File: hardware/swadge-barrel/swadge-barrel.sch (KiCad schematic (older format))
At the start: 48 parts, among them J1 USB_B_Micro, Q1 Q_NPN_BEC, SW1 SW_SPDT, U1 ESP-13-WROOM-02D, U2 OLED_DISPLAY, U3 BUS_PCIexpress, U4 QMA6981, U5 AP1117-33, U6 OLED_CONNECTOR

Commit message: Barrel BOM
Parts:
- C4, C5, C6, C9: Notes 1206 Package, must be at least 1.5mm tall, may be taller. 1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 -> 1206 Package. must be at least 1.5mm tall. may be taller. 1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
- D1, D2, D3, D4, D5, D6: Notes Use WS2812B LED, Digikey item is x10 -> Use WS2812B LED. Digikey item is x10
- LS1: Digikey https://lcsc.com/product-detail/Buzzers_Jiangsu-Huaneng-Ele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 -> LCSC Part #C96102; Notes Use magnetic buzzer, 3V rated, 9mm diameter, 5mm between th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 -> Use magnetic buzzer. 3V rated. 9mm diameter. 5mm between th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
- Q1: Notes Use any NPN transistor in SOT-23 package with the same leads as BC848BLT3G (1=base, 2=emitter, 3=collector) -> Use any NPN transistor in SOT-23 package with the same leads as BC848BLT3G (1=base. 2=emitter. 3=collector)
- R8, R9: Notes 0603 Package, must not be taller than 0.8mm, this sits unde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 -> 0603 Package. must not be taller than 0.8mm. this sits unde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
- S2, S3: Digikey https://www.digikey.com/product-detail/en/omron-electronics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 -> SW1278CT-ND
- U2: Notes Must be a single color, white. Must have SSD1306 driver. Mu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 -> Must be a single color. white. Must have SSD1306 driver. Mu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
- U6: Notes Must have top contacts, same as the OLED -> Must have top contacts. same as the OLED
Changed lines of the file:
@@
 EESchema Schematic File Version 4
-LIBS:swadge-barrel-cache
 EELAYER 29 0
 EELAYER END
@@
 F 4 "45" H 0   0   50  0001 C CNN "Cost100"
 F 5 "1528-1104-ND" H 0   0   50  0001 C CNN "Digikey"
-F 6 "Use WS2812B LED, Digikey item is x10" H 0   0   50  0001 C CNN "Notes"
+F 6 "Use WS2812B LED. Digikey item is x10" H 0   0   50  0001 C CNN "Notes"
 F 7 "Y" H 0   0   50  0001 C CNN "Substitutable"
 	1    4300 1650
@@
 F 4 "45" H 0   0   50  0001 C CNN "Cost100"
 F 5 "1528-1104-ND" H 0   0   50  0001 C CNN "Digikey"
-F 6 "Use WS2812B LED, Digikey item is x10" H 0   0   50  0001 C CNN "Notes"
+F 6 "Use WS2812B LED. Digikey item is x10" H 0   0   50  0001 C CNN "Notes"
 F 7 "Y" H 0   0   50  0001 C CNN "Substitutable"
 	1    4950 1650
@@
 F 4 "45" H 0   0   50  0001 C CNN "Cost100"
 F 5 "1528-1104-ND" H 0   0   50  0001 C CNN "Digikey"
-F 6 "Use WS2812B LED, Digikey item is x10" H 0   0   50  0001 C CNN "Notes"
+F 6 "Use WS2812B LED. Digikey item is x10" H 0   0   50  0001 C CNN "Notes"
 F 7 "Y" H 0   0   50  0001 C CNN "Substitutable"
 	1    5600 1650
@@
 F 4 "45" H 0   0   50  0001 C CNN "Cost100"
 F 5 "1528-1104-ND" H 0   0   50  0001 C CNN "Digikey"
-F 6 "Use WS2812B LED, Digikey item is x10" H 0   0   50  0001 C CNN "Notes"
+F 6 "Use WS2812B LED. Digikey item is x10" H 0   0   50  0001 C CNN "Notes"
 F 7 "Y" H 0   0   50  0001 C CNN "Substitutable"
 	1    6250 1650
@@
 F 4 "45" H 0   0   50  0001 C CNN "Cost100"
 F 5 "1528-1104-ND" H 0   0   50  0001 C CNN "Digikey"
-F 6 "Use WS2812B LED, Digikey item is x10" H 0   0   50  0001 C CNN "Notes"
+F 6 "Use WS2812B LED. Digikey item is x10" H 0   0   50  0001 C CNN "Notes"
 F 7 "Y" H 0   0   50  0001 C CNN "Substitutable"
 	1    6900 1650
@@
 F 4 "45" H 0   0   50  0001 C CNN "Cost100"
 F 5 "1528-1104-ND" H 0   0   50  0001 C CNN "Digikey"
-F 6 "Use WS2812B LED, Digikey item is x10" H 0   0   50  0001 C CNN "Notes"
+F 6 "Use WS2812B LED. Digikey item is x10" H 0   0   50  0001 C CNN "Notes"
 F 7 "Y" H 0   0   50  0001 C CNN "Substitutable"
 	1    7550 1650
@@
 F 5 "1276-1097-1-ND" H 0   0   50  0001 C CNN "Digikey"
 F 6 "Y" H 0   0   50  0001 C CNN "Substitutable"
-F 7 "1206 Package, must be at least 1.5mm tall, may be taller. 1.8mm is common and preferrable. This protects the OLED's corners" H 4150 3600 50  0001 C CNN "Notes"
+F 7 "1206 Package. must be at least 1.5mm tall. may be taller. 1.8mm is common and preferable. This protects the OLED's corners" H 4150 3600 50  0001 C CNN "Notes"
 	1    4150 3600
 	-1   0    0    1
@@
 F 5 "1276-1097-1-ND" H 0   0   50  0001 C CNN "Digikey"
 F 6 "Y" H 0   0   50  0001 C CNN "Substitutable"
-F 7 "1206 Package, must be at least 1.5mm tall, may be taller. 1.8mm is common and preferrable. This protects the OLED's corners" H 4000 3300 50  0001 C CNN "Notes"
+F 7 "1206 Package. must be at least 1.5mm tall. may be taller. 1.8mm is common and preferable. This protects the OLED's corners" H 4000 3300 50  0001 C CNN "Notes"
 	1    4000 3300
 	-1   0    0    1
@@
 F 5 "1276-1097-1-ND" H 0   0   50  0001 C CNN "Digikey"
 F 6 "Y" H 0   0   50  0001 C CNN "Substitutable"
-F 7 "1206 Package, must be at least 1.5mm tall, may be taller. 1.8mm is common and preferrable. This protects the OLED's corners" H 4450 2700 50  0001 C CNN "Notes"
+F 7 "1206 Package. must be at least 1.5mm tall. may be taller. 1.8mm is common and preferable. This protects the OLED's corners" H 4450 2700 50  0001 C CNN "Notes"
 	1    4450 2700
 	1    0    0    -1
@@
 F 5 "1276-1097-1-ND" H 0   0   50  0001 C CNN "Digikey"
 F 6 "Y" H 0   0   50  0001 C CNN "Substitutable"
-F 7 "1206 Package, must be at least 1.5mm tall, may be taller. 1.8mm is common and preferrable. This protects the OLED's corners" H 4050 2900 50  0001 C CNN "Notes"
+F 7 "1206 Package. must be at least 1.5mm tall. may be taller. 1.8mm is common and preferable. This protects the OLED's corners" H 4050 2900 50  0001 C CNN "Notes"
 	1    4050 2900
 	1    0    0    -1
@@
 F 1 "B3FS-4002P" H 2775 1284 50  0000 C CNN
 F 2 "Swadge_Parts:B3FS4002P" H 2750 1600 50  0001 L CNN
-F 3 "http://omronfs.omron.com/en_US/ecb/products/pdf/en-b3fs_4.pdf" H 3100 1150 50  0001 L CNN
-F 4 "https://www.digikey.com/product-detail/en/omron-electronics-inc-emc-div/B3FS-4002P/SW1278TR-ND/2772023" H 2800 1750 50  0001 C CNN "Digikey"
+F 3 "https://omronfs.omron.com/en_US/ecb/products/pdf/en-b3fs_4.pdf" H 3100 1150 50  0001 L CNN
+F 4 "SW1278CT-ND" H 2800 1750 50  0001 C CNN "Digikey"
 F 5 "76" H 2600 1600 50  0001 C CNN "Cost100"
 F 6 "Y" H 2450 1650 50  0001 C CNN "Substitutable"
@@
 F 1 "B3FS-4002P" H 1425 1284 50  0000 C CNN
 F 2 "Swadge_Parts:B3FS4002P" H 1400 1600 50  0001 L CNN
-F 3 "http://omronfs.omron.com/en_US/ecb/products/pdf/en-b3fs_4.pdf" H 1750 1150 50  0001 L CNN
-F 4 "https://www.digikey.com/product-detail/en/omron-electronics-inc-emc-div/B3FS-4002P/SW1278TR-ND/2772023" H 1450 1750 50  0001 C CNN "Digikey"
+F 3 "https://omronfs.omron.com/en_US/ecb/products/pdf/en-b3fs_4.pdf" H 1750 1150 50  0001 L CNN
+F 4 "SW1278CT-ND" H 1450 1750 50  0001 C CNN "Digikey"
 F 5 "76" H 1250 1600 50  0001 C CNN "Cost100"
 F 6 "Y" H 1100 1650 50  0001 C CNN "Substitutable"
@@
 F 5 "1.554" H 1750 7400 50  0001 C CNN "Cost100"
 F 6 "Y" H 1700 7500 50  0001 C CNN "Substitutable"
-F 7 "Use any NPN transistor in SOT-23 package with the same leads as BC848BLT3G (1=base, 2=emitter, 3=collector)" H 1400 6950 50  0001 C CNN "Notes"
+F 7 "Use any NPN transistor in SOT-23 package with the same leads as BC848BLT3G (1=base. 2=emitter. 3=collector)" H 1400 6950 50  0001 C CNN "Notes"
 	1    1400 6950
 	1    0    0    -1
@@
 F 2 "Swadge_Parts:Buzzer_12x9.5RM7.6" H 1700 6350 50  0001 C CNN
 F 3 "https://datasheet.lcsc.com/szlcsc/Jiangsu-Huaneng-Elec-HNB09A03_C96102.pdf" H 1690 6500 50  0001 C CNN
-F 4 "https://lcsc.com/product-detail/Buzzers_Jiangsu-Huaneng-Elec-HNB09A03_C96102.html" H 1300 6900 50  0001 C CNN "Digikey"
+F 4 "LCSC Part #C96102" H 1300 6900 50  0001 C CNN "Digikey"
 F 5 "13.48" H 1950 6800 50  0001 C CNN "Cost100"
 F 6 "Y" H 1950 7050 50  0001 C CNN "Substitutable"
-F 7 "Use magnetic buzzer, 3V rated, 9mm diameter, 5mm between the leads" H 1400 7000 50  0001 C CNN "Notes"
+F 7 "Use magnetic buzzer. 3V rated. 9mm diameter. 5mm between the leads" H 1400 7000 50  0001 C CNN "Notes"
 	1    1700 6550
 	1    0    0    -1
@@
 F 5 "10" H 2600 6400 10  0001 C CNN "Cost100"
 F 6 "Y" H 2600 6400 10  0001 C CNN "Substitutable"
-F 7 "0603 Package, must not be taller than 0.8mm, this sits under part of the OLED" H 2600 6400 50  0001 C CNN "Notes"
+F 7 "0603 Package. must not be taller than 0.8mm. this sits under part of the OLED" H 2600 6400 50  0001 C CNN "Notes"
 	1    2600 6400
 	1    0    0    -1
@@
 F 5 "10" H 2950 6400 10  0001 C CNN "Cost100"
 F 6 "Y" H 2950 6400 10  0001 C CNN "Substitutable"
-F 7 "0603 Package, must not be taller than 0.8mm, this sits under part of the OLED" H 2950 6400 50  0001 C CNN "Notes"
+F 7 "0603 Package. must not be taller than 0.8mm. this sits under part of the OLED" H 2950 6400 50  0001 C CNN "Notes"
 	1    2950 6400
 	1    0    0    -1
@@
 F 5 "LCSC #C11095" H 0   0   50  0001 C CNN "Digikey"
 F 6 "Y" H 0   0   50  0001 C CNN "Substitutable"
-F 7 "Must have top contacts, same as the OLED" H 5950 4050 50  0001 C CNN "Notes"
+F 7 "Must have top contacts. same as the OLED" H 5950 4050 50  0001 C CNN "Notes"
 	1    5950 4050
 	1    0    0    -1
@@
 F 6 "352" H 5100 6500 50  0001 C CNN "Cost100"
 F 7 "Y" H 5100 6500 50  0001 C CNN "Substitutable"
-F 8 "Must be a single color, white. Must have SSD1306 driver. Must have top pins, 0.5mm pitch, like the connector" H 5100 6500 50  0001 C CNN "Notes"
+F 8 "Must be a single color. white. Must have SSD1306 driver. Must have top pins. 0.5mm pitch. like the connector" H 5100 6500 50  0001 C CNN "Notes"
 	1    5100 6500
 	1    0    0    -1

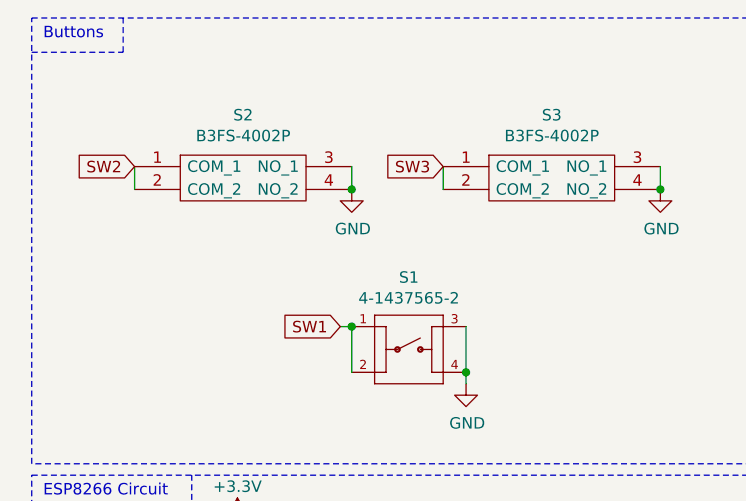
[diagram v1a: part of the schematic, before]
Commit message: #26 Remapped buttons to match devkit gpios
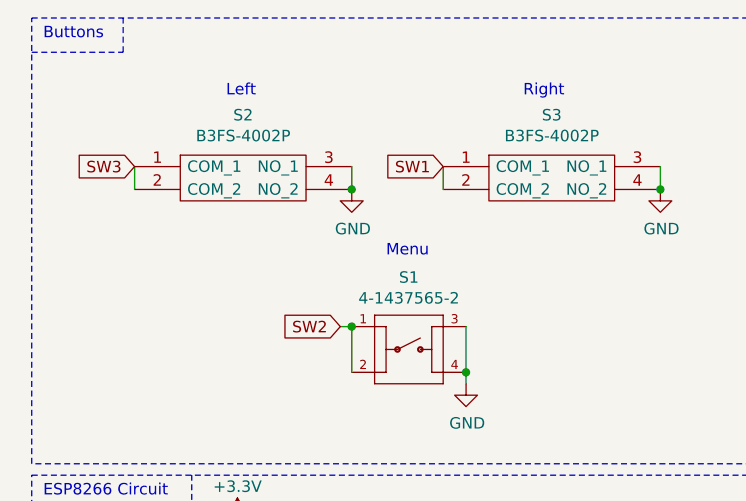
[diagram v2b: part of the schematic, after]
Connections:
- net SW1: now also S3.1 (COM_1), S3.2 (COM_2); no longer S1.1, S1.2
- net SW2: now also S1.1, S1.2; no longer S2.1 (COM_1), S2.2 (COM_2)
- net SW3: now also S2.1 (COM_1), S2.2 (COM_2); no longer S3.1 (COM_1), S3.2 (COM_2)
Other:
- note added: "Left"
- note added: "Menu"
- note added: "Right"
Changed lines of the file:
@@
 EESchema Schematic File Version 4
+LIBS:swadge-barrel-cache
 EELAYER 29 0
 EELAYER END
@@
 Wire Notes Line
 	10000 650  10000 500
-Text GLabel 1850 1850 0    50   Input ~ 0
+Text GLabel 2300 1150 0    50   Input ~ 0
 SW1
 $Comp
@@
 	1    0    0    -1
 $EndComp
-Text GLabel 2300 1150 0    50   Input ~ 0
+Text GLabel 950  1150 0    50   Input ~ 0
 SW3
-Text GLabel 950  1150 0    50   Input ~ 0
+Text GLabel 1850 1850 0    50   Input ~ 0
 SW2
 Connection ~ 1900 1850
@@
 	1    0    0    -1
 $EndComp
+Text Notes 1350 850  0    50   ~ 0
+Left
+Text Notes 2650 850  0    50   ~ 0
+Right
+Text Notes 2050 1550 0    50   ~ 0
+Menu
 $EndSCHEMATC

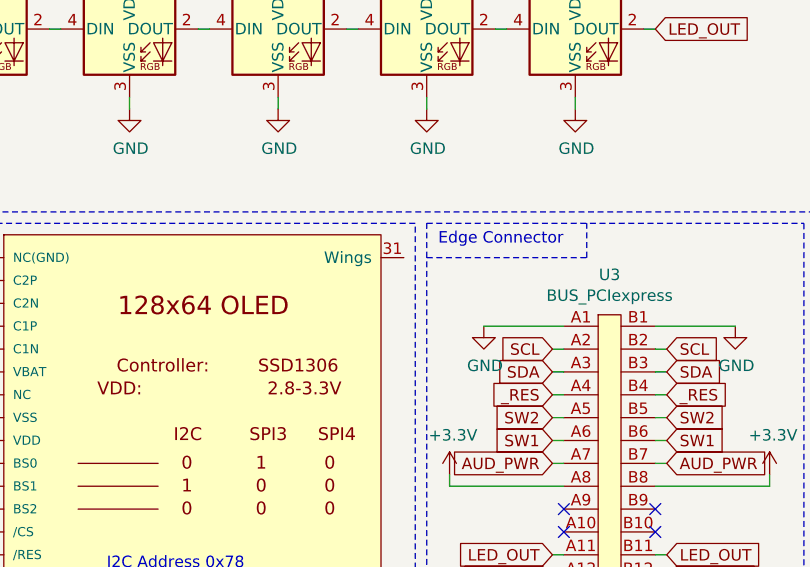
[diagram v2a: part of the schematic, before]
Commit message: Flipped OLED contacts, haven't routed them yet #24
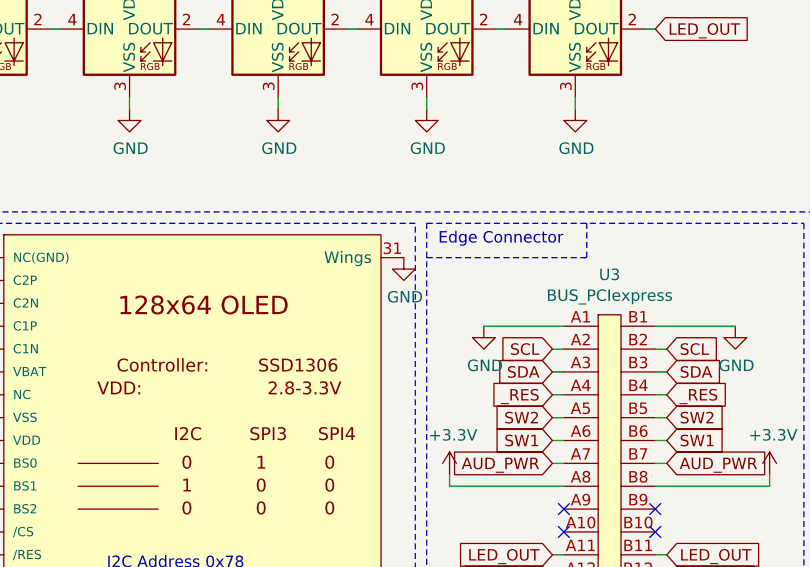
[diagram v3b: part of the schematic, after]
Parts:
- U6: footprint Swadge_Parts:oled-flat_copy -> Swadge_Parts:ER-OLED0.96-1.3
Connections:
- net GND: now also U6.31 (Wings)
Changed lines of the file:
@@
 F 0 "U6" H 5100 2300 45  0000 L CNN
 F 1 "OLED_CONNECTOR" H 5100 2400 45  0000 L CNN
-F 2 "Swadge_Parts:oled-flat_copy" H 5980 4200 20  0001 C CNN
+F 2 "Swadge_Parts:ER-OLED0.96-1.3" H 5980 4200 20  0001 C CNN
 F 3 "https://datasheet.lcsc.com/szlcsc/JUSHUO-AFC07-S30ECC-00_C11095.pdf" H 5950 4050 50  0001 C CNN
 F 4 "119" H 0   0   50  0001 C CNN "Cost100"
@@
 Text Notes 2050 1550 0    50   ~ 0
 Menu
+$Comp
+L power:GND #PWR?
+U 1 1 5D809654
+P 6800 2650
+F 0 "#PWR?" H 6800 2400 50  0001 C CNN
+F 1 "GND" H 6805 2477 50  0000 C CNN
+F 2 "" H 6800 2650 50  0001 C CNN
+F 3 "" H 6800 2650 50  0001 C CNN
+	1    6800 2650
+	1    0    0    -1
+$EndComp
 $EndSCHEMATC

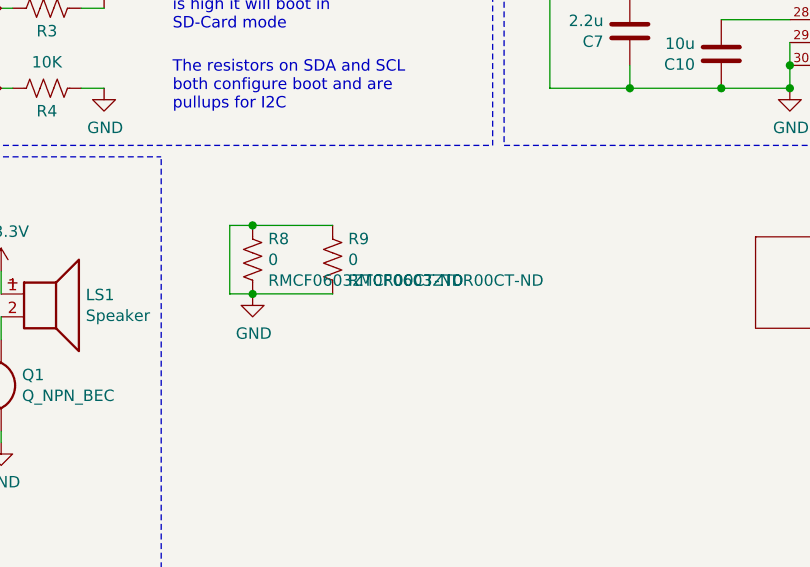
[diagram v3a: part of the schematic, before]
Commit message: #24 Rerouted OLED traces
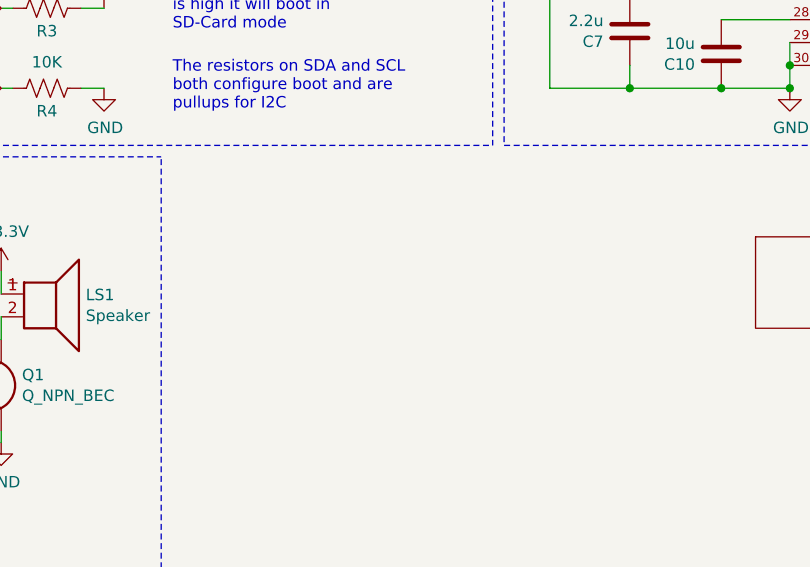
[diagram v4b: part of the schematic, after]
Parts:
- removed R8, R9: 0, Swadge_Parts:R_0603_1608Metric, symbol Swadge_Parts:R_US
- C4, C5, C6, C9: footprint Swadge_Parts:C_1206_3216Metric -> Swadge_Parts:C_0603_1608Metric; Digikey 1276-1097-1-ND -> 1276-1036-1-ND; Notes 1206 Package. must be at least 1.5mm tall. may be taller. 1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 -> 0603 Package
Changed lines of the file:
@@
 F 0 "C6" H 3850 3650 50  0000 L CNN
 F 1 "1u" H 3850 3550 50  0000 L CNN
-F 2 "Swadge_Parts:C_1206_3216Metric" H 4188 3450 50  0001 C CNN
+F 2 "Swadge_Parts:C_0603_1608Metric" H 4188 3450 50  0001 C CNN
 F 3 "" H 4150 3600 50  0001 C CNN
 F 4 "10" H 0   0   50  0001 C CNN "Cost100"
-F 5 "1276-1097-1-ND" H 0   0   50  0001 C CNN "Digikey"
+F 5 "1276-1036-1-ND" H 0   0   50  0001 C CNN "Digikey"
 F 6 "Y" H 0   0   50  0001 C CNN "Substitutable"
-F 7 "1206 Package. must be at least 1.5mm tall. may be taller. 1.8mm is common and preferable. This protects the OLED's corners" H 4150 3600 50  0001 C CNN "Notes"
+F 7 "0603 Package" H 4150 3600 50  0001 C CNN "Notes"
 	1    4150 3600
 	-1   0    0    1
@@
 F 0 "C4" H 4115 3346 50  0000 L CNN
 F 1 "1u" H 4115 3255 50  0000 L CNN
-F 2 "Swadge_Parts:C_1206_3216Metric" H 4038 3150 50  0001 C CNN
+F 2 "Swadge_Parts:C_0603_1608Metric" H 4038 3150 50  0001 C CNN
 F 3 "" H 4000 3300 50  0001 C CNN
 F 4 "10" H 0   0   50  0001 C CNN "Cost100"
-F 5 "1276-1097-1-ND" H 0   0   50  0001 C CNN "Digikey"
+F 5 "1276-1036-1-ND" H 0   0   50  0001 C CNN "Digikey"
 F 6 "Y" H 0   0   50  0001 C CNN "Substitutable"
-F 7 "1206 Package. must be at least 1.5mm tall. may be taller. 1.8mm is common and preferable. This protects the OLED's corners" H 4000 3300 50  0001 C CNN "Notes"
+F 7 "0603 Package" H 4000 3300 50  0001 C CNN "Notes"
 	1    4000 3300
 	-1   0    0    1
@@
 F 0 "C9" H 4565 2746 50  0000 L CNN
 F 1 "1u" H 4565 2655 50  0000 L CNN
-F 2 "Swadge_Parts:C_1206_3216Metric" H 4488 2550 50  0001 C CNN
+F 2 "Swadge_Parts:C_0603_1608Metric" H 4488 2550 50  0001 C CNN
 F 3 "" H 4450 2700 50  0001 C CNN
 F 4 "10" H 0   0   50  0001 C CNN "Cost100"
-F 5 "1276-1097-1-ND" H 0   0   50  0001 C CNN "Digikey"
+F 5 "1276-1036-1-ND" H 0   0   50  0001 C CNN "Digikey"
 F 6 "Y" H 0   0   50  0001 C CNN "Substitutable"
-F 7 "1206 Package. must be at least 1.5mm tall. may be taller. 1.8mm is common and preferable. This protects the OLED's corners" H 4450 2700 50  0001 C CNN "Notes"
+F 7 "0603 Package" H 4450 2700 50  0001 C CNN "Notes"
 	1    4450 2700
 	1    0    0    -1
@@
 F 0 "C5" H 4165 2946 50  0000 L CNN
 F 1 "1u" H 4165 2855 50  0000 L CNN
-F 2 "Swadge_Parts:C_1206_3216Metric" H 4088 2750 50  0001 C CNN
+F 2 "Swadge_Parts:C_0603_1608Metric" H 4088 2750 50  0001 C CNN
 F 3 "" H 4050 2900 50  0001 C CNN
 F 4 "10" H 0   0   50  0001 C CNN "Cost100"
-F 5 "1276-1097-1-ND" H 0   0   50  0001 C CNN "Digikey"
+F 5 "1276-1036-1-ND" H 0   0   50  0001 C CNN "Digikey"
 F 6 "Y" H 0   0   50  0001 C CNN "Substitutable"
-F 7 "1206 Package. must be at least 1.5mm tall. may be taller. 1.8mm is common and preferable. This protects the OLED's corners" H 4050 2900 50  0001 C CNN "Notes"
+F 7 "0603 Package" H 4050 2900 50  0001 C CNN "Notes"
 	1    4050 2900
 	1    0    0    -1
@@
 Wire Notes Line
 	500  7750 2200 7750
-$Comp
-L Swadge_Parts:R_US R8
-U 1 1 5D6E1A5B
-P 2600 6400
-F 0 "R8" H 2668 6491 50  0000 L CNN
-F 1 "0" H 2668 6400 50  0000 L CNN
-F 2 "Swadge_Parts:R_0603_1608Metric" V 2640 6390 50  0001 C CNN
-F 3 "~" V 2700 6400 50  0001 C CNN
-F 4 "RMCF0603ZT0R00CT-ND" H 2668 6309 50  0000 L CNN "Digikey"
-F 5 "10" H 2600 6400 10  0001 C CNN "Cost100"
-F 6 "Y" H 2600 6400 10  0001 C CNN "Substitutable"
-F 7 "0603 Package. must not be taller than 0.8mm. this sits under part of the OLED" H 2600 6400 50  0001 C CNN "Notes"
-	1    2600 6400
-	1    0    0    -1
-$EndComp
-$Comp
-L Swadge_Parts:R_US R9
-U 1 1 5D6E3BEA
-P 2950 6400
-F 0 "R9" H 3018 6491 50  0000 L CNN
-F 1 "0" H 3018 6400 50  0000 L CNN
-F 2 "Swadge_Parts:R_0603_1608Metric" V 2990 6390 50  0001 C CNN
-F 3 "~" V 3050 6400 50  0001 C CNN
-F 4 "RMCF0603ZT0R00CT-ND" H 3018 6309 50  0000 L CNN "Digikey"
-F 5 "10" H 2950 6400 10  0001 C CNN "Cost100"
-F 6 "Y" H 2950 6400 10  0001 C CNN "Substitutable"
-F 7 "0603 Package. must not be taller than 0.8mm. this sits under part of the OLED" H 2950 6400 50  0001 C CNN "Notes"
-	1    2950 6400
-	1    0    0    -1
-$EndComp
-Wire Wire Line
-	2950 6250 2600 6250
-Wire Wire Line
-	2950 6550 2600 6550
-Wire Wire Line
-	2600 6550 2500 6550
-Wire Wire Line
-	2500 6550 2500 6250
-Wire Wire Line
-	2500 6250 2600 6250
-Connection ~ 2600 6550
-Connection ~ 2600 6250
-$Comp
-L power:GND #PWR049
-U 1 1 5D712417
-P 2600 6550
-F 0 "#PWR049" H 2600 6300 50  0001 C CNN
-F 1 "GND" H 2605 6377 50  0000 C CNN
-F 2 "" H 2600 6550 50  0001 C CNN
-F 3 "" H 2600 6550 50  0001 C CNN
-	1    2600 6550
-	1    0    0    -1
-$EndComp
 Text GLabel 7900 1650 2    50   Input ~ 0
 LED_OUT
@@
 Menu
 $Comp
-L power:GND #PWR?
+L power:GND #PWR0103
 U 1 1 5D809654
 P 6800 2650
-F 0 "#PWR?" H 6800 2400 50  0001 C CNN
+F 0 "#PWR0103" H 6800 2400 50  0001 C CNN
 F 1 "GND" H 6805 2477 50  0000 C CNN
 F 2 "" H 6800 2650 50  0001 C CNN
